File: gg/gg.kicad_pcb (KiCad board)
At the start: 2 copper layers, 59 x 26 mm, 3 parts, among them J1 Game Gear, J2 Game Gear

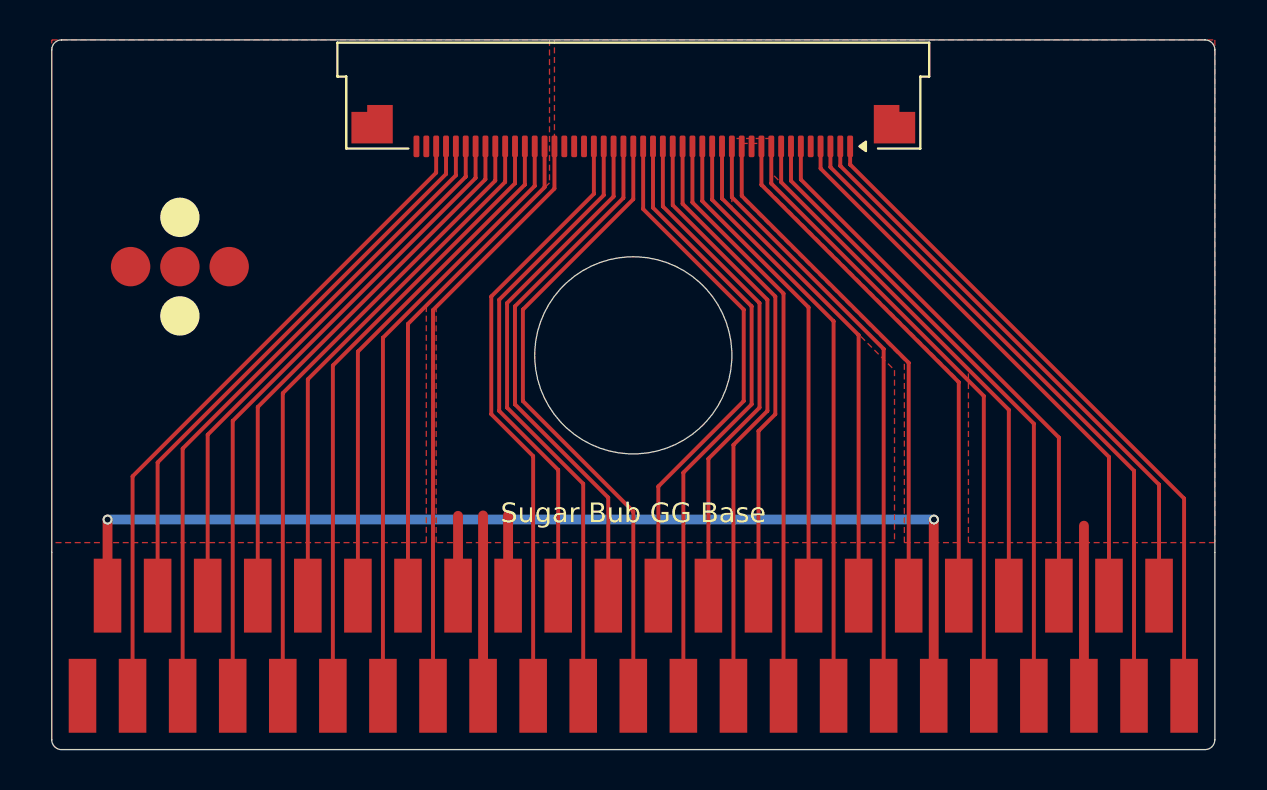
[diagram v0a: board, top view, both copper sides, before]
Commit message: Widen GG cart edge footprint and add holes
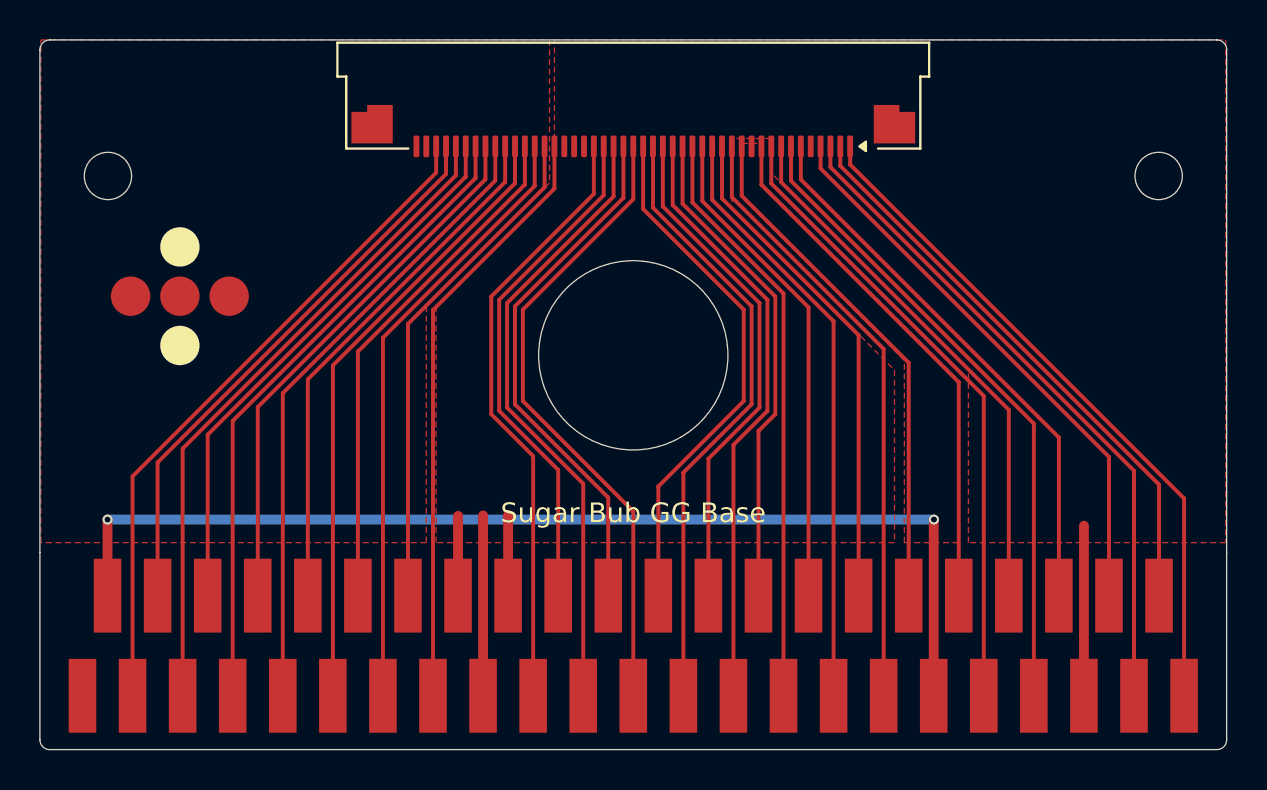
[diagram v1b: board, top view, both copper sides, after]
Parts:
- moved TP1 1.50 mm to (77.0, 87.0)
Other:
- board size 59 x 26 mm -> 60.2 x 30.3 mm
- board text added: "Finish: ENIG Thickness: 1.0mm"
- board text removed: "Finish: ENIG Thickness: 0.8mm"
